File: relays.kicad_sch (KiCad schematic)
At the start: 8 parts, among them K1 J107F1AS123VDC.36, K2 J107F1AS123VDC.36, K3 J107F1AS123VDC.36, Q1 2N2222A, Q2 2N2222A, Q3 2N2222A

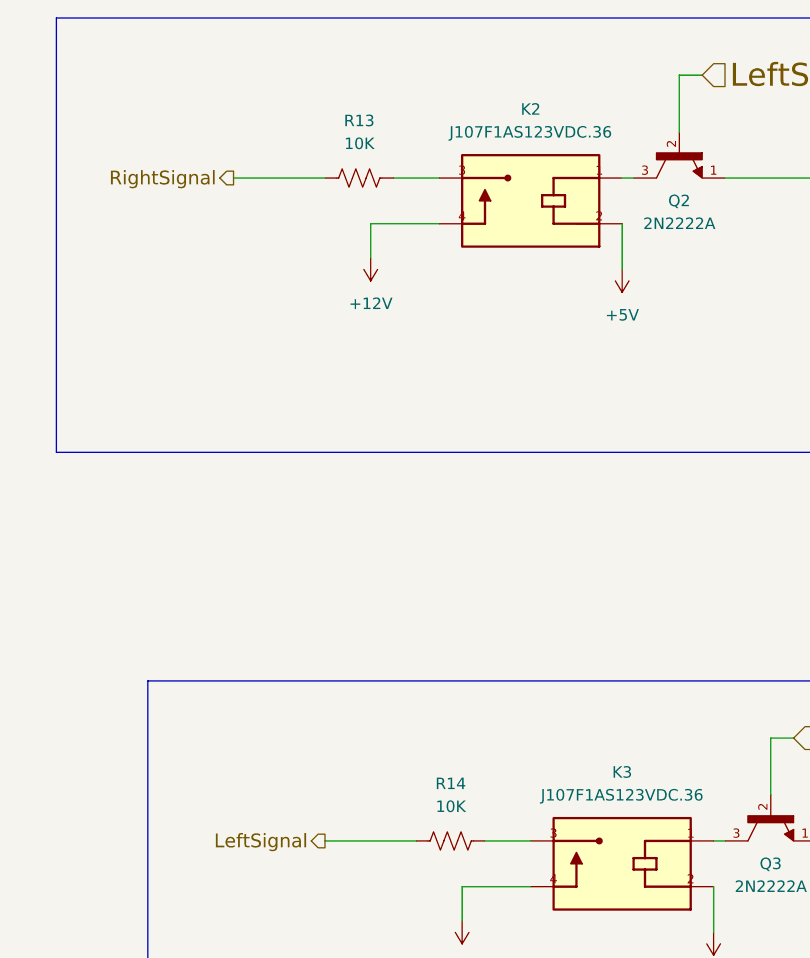
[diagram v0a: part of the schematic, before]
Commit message: placed most components
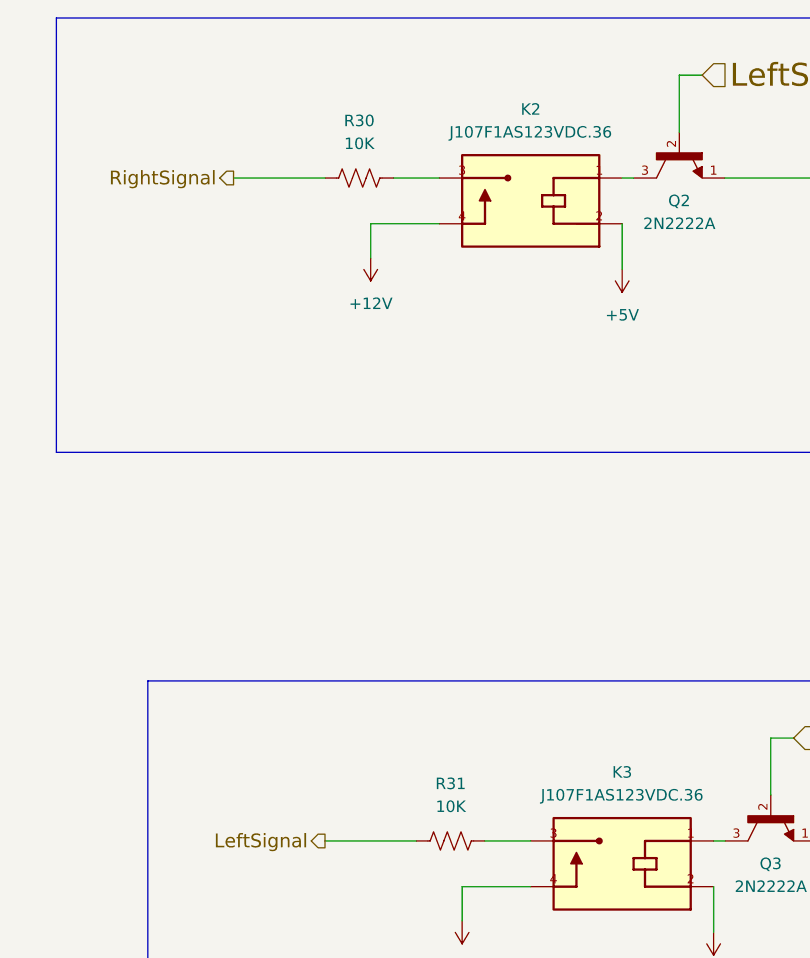
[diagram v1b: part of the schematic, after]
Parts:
- R30: renamed from R13; footprint (none) -> Resistor_SMD:R_0805_2012Metric
- R31: renamed from R14; footprint (none) -> Resistor_SMD:R_0805_2012Metric
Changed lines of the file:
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@@
 		(dnp no)
 		(fields_autoplaced yes)
-		(property "Reference" "#PWR023"
+		(property "Reference" "#PWR051"
 			(at 86.36 55.88 0)
 			(effects
@@
 			(project "Main-Board-V2"
 				(path "/c01682a2-308a-4674-9b8f-80e441c05d08/21d63675-f3e4-4d8d-ac51-eab9a4aeae5e"
-					(reference "#PWR023")
+					(reference "#PWR051")
 					(unit 1)
 				)
@@
 		(dnp no)
 		(fields_autoplaced yes)
-		(property "Reference" "#PWR025"
+		(property "Reference" "#PWR052"
 			(at 109.22 59.69 0)
 			(effects
@@
 			(project "Main-Board-V2"
 				(path "/c01682a2-308a-4674-9b8f-80e441c05d08/21d63675-f3e4-4d8d-ac51-eab9a4aeae5e"
-					(reference "#PWR025")
+					(reference "#PWR052")
 					(unit 1)
 				)
@@
 		(dnp no)
 		(fields_autoplaced yes)
-		(property "Reference" "R13"
+		(property "Reference" "R30"
 			(at 185.42 41.91 90)
 			(effects
@@
 			)
 		)
-		(property "Footprint" ""
+		(property "Footprint" "Resistor_SMD:R_0805_2012Metric"
 			(at 185.674 47.244 90)
 			(effects
@@
 			(project "Main-Board-V2"
 				(path "/c01682a2-308a-4674-9b8f-80e441c05d08/21d63675-f3e4-4d8d-ac51-eab9a4aeae5e"
-					(reference "R13")
+					(reference "R30")
 					(unit 1)
 				)
@@
 		(dnp no)
 		(fields_autoplaced yes)
-		(property "Reference" "#PWR029"
+		(property "Reference" "#PWR056"
 			(at 224.79 128.27 0)
 			(effects
@@
 			(project "Main-Board-V2"
 				(path "/c01682a2-308a-4674-9b8f-80e441c05d08/21d63675-f3e4-4d8d-ac51-eab9a4aeae5e"
-					(reference "#PWR029")
+					(reference "#PWR056")
 					(unit 1)
 				)
@@
 		(dnp no)
 		(fields_autoplaced yes)
-		(property "Reference" "#PWR044"
+		(property "Reference" "#PWR057"
 			(at 237.49 58.42 0)
 			(effects
@@
 			(project "Main-Board-V2"
 				(path "/c01682a2-308a-4674-9b8f-80e441c05d08/21d63675-f3e4-4d8d-ac51-eab9a4aeae5e"
-					(reference "#PWR044")
+					(reference "#PWR057")
 					(unit 1)
 				)
@@
 		(dnp no)
 		(fields_autoplaced yes)
-		(property "Reference" "#PWR028"
+		(property "Reference" "#PWR055"
 			(at 214.63 54.61 0)
 			(effects
@@
 			(project "Main-Board-V2"
 				(path "/c01682a2-308a-4674-9b8f-80e441c05d08/21d63675-f3e4-4d8d-ac51-eab9a4aeae5e"
-					(reference "#PWR028")
+					(reference "#PWR055")
 					(unit 1)
 				)
@@
 		(dnp no)
 		(fields_autoplaced yes)
-		(property "Reference" "#PWR045"
+		(property "Reference" "#PWR058"
 			(at 247.65 132.08 0)
 			(effects
@@
 			(project "Main-Board-V2"
 				(path "/c01682a2-308a-4674-9b8f-80e441c05d08/21d63675-f3e4-4d8d-ac51-eab9a4aeae5e"
-					(reference "#PWR045")
+					(reference "#PWR058")
 					(unit 1)
 				)
@@
 		(dnp no)
 		(fields_autoplaced yes)
-		(property "Reference" "R14"
+		(property "Reference" "R31"
 			(at 195.58 115.57 90)
 			(effects
@@
 			)
 		)
-		(property "Footprint" ""
+		(property "Footprint" "Resistor_SMD:R_0805_2012Metric"
 			(at 195.834 120.904 90)
 			(effects
@@
 			(project "Main-Board-V2"
 				(path "/c01682a2-308a-4674-9b8f-80e441c05d08/21d63675-f3e4-4d8d-ac51-eab9a4aeae5e"
-					(reference "R14")
+					(reference "R31")
 					(unit 1)
 				)
@@
 		(dnp no)
 		(fields_autoplaced yes)
-		(property "Reference" "#PWR026"
+		(property "Reference" "#PWR053"
 			(at 186.69 53.34 0)
 			(effects
@@
 			(project "Main-Board-V2"
 				(path "/c01682a2-308a-4674-9b8f-80e441c05d08/21d63675-f3e4-4d8d-ac51-eab9a4aeae5e"
-					(reference "#PWR026")
+					(reference "#PWR053")
 					(unit 1)
 				)
@@
 		(dnp no)
 		(fields_autoplaced yes)
-		(property "Reference" "#PWR027"
+		(property "Reference" "#PWR054"
 			(at 196.85 127 0)
 			(effects
@@
 			(project "Main-Board-V2"
 				(path "/c01682a2-308a-4674-9b8f-80e441c05d08/21d63675-f3e4-4d8d-ac51-eab9a4aeae5e"
-					(reference "#PWR027")
+					(reference "#PWR054")
 					(unit 1)
 				)

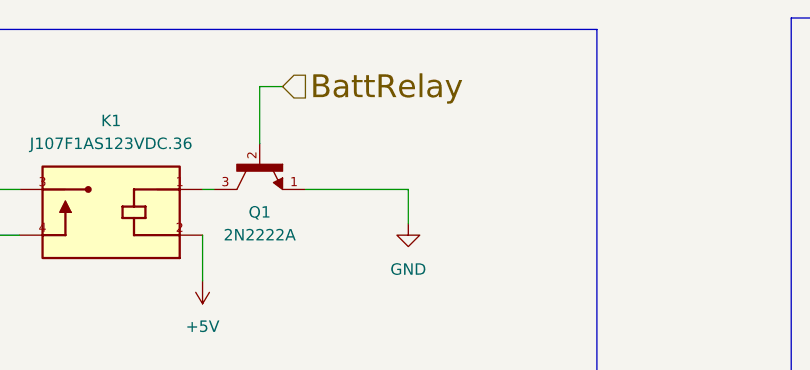
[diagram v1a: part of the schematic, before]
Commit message: replaced CAN chip, power planes
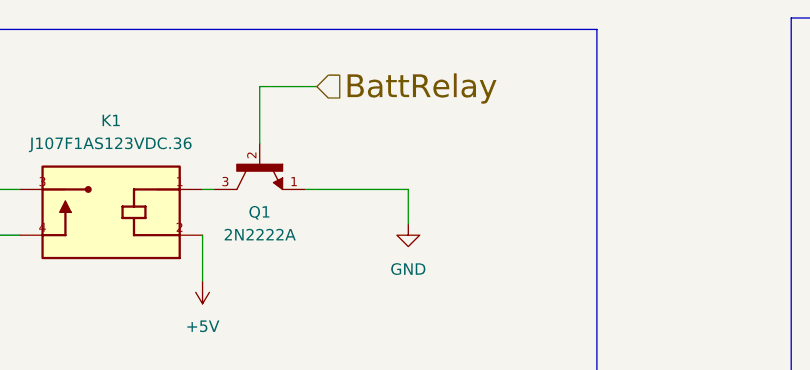
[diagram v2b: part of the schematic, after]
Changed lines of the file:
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@@
 	(wire
 		(pts
-			(xy 92.71 38.1) (xy 95.25 38.1)
+			(xy 92.71 38.1) (xy 99.06 38.1)
 		)
 		(stroke
@@
 	(hierarchical_label "BattRelay"
 		(shape input)
-		(at 95.25 38.1 0)
+		(at 99.06 38.1 0)
 		(effects
 			(font

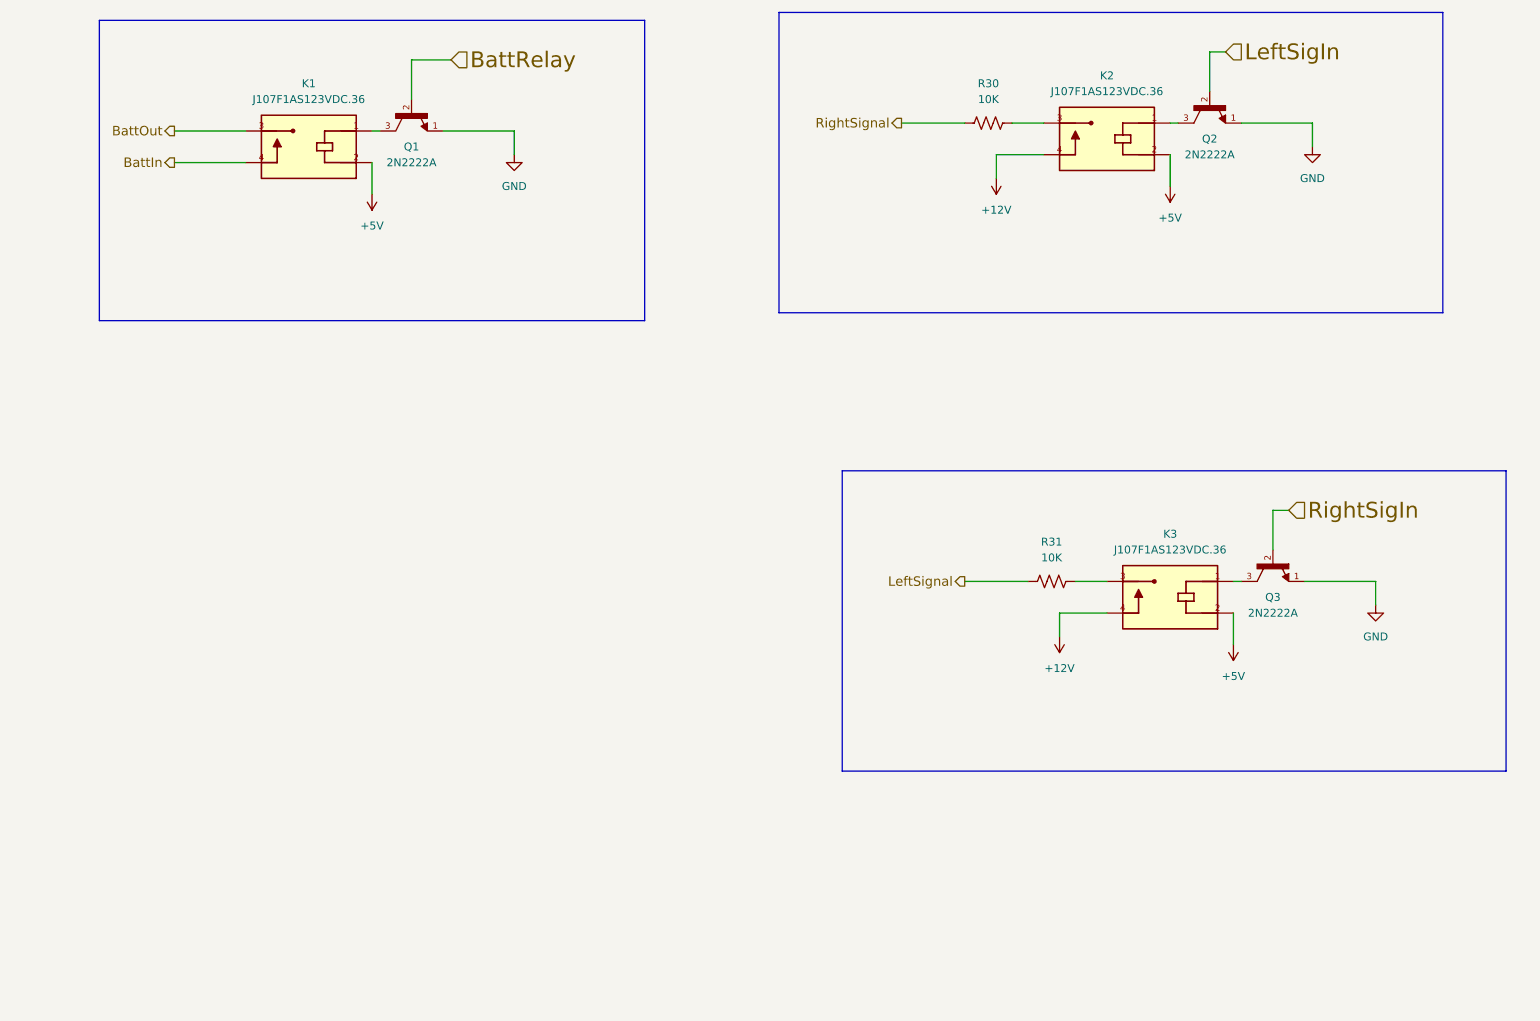
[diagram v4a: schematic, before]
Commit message: redid 35 pos pinout
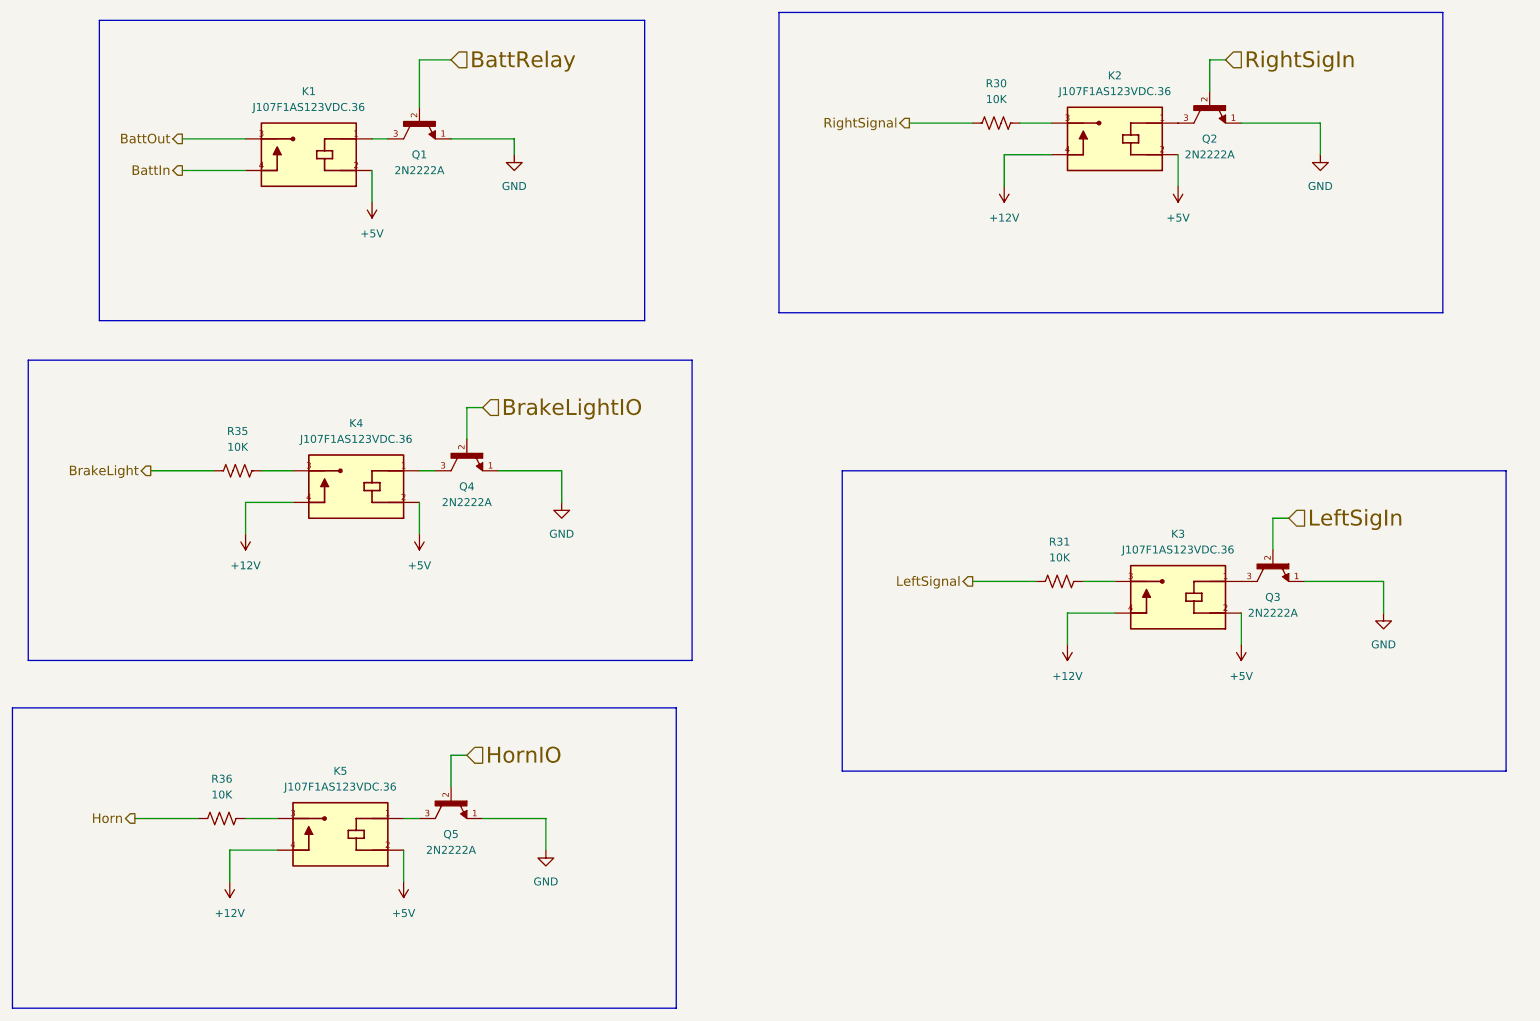
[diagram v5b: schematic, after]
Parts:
- added K4, K5: J107F1AS123VDC.36, PRE29-5V-S-450-1A-E:RELAY_PRE29-5V-S-450-1A-E, symbol PRE29-5V-S-450-1A-E:PRE29-5V-S-450-1A-E
- added Q4, Q5: 2N2222A, 2N2222A:TO92254P470H750-3, symbol 2N2222A:2N2222A
- added R35, R36: 10K, Resistor_SMD:R_0805_2012Metric, symbol Device:R_US
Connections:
- net +12V: now also K4.4, K5.4
- net +5V: now also K4.2, K5.2
- net GND: now also Q4.1, Q5.1
- net LeftSigIn: now also Q3.2; no longer Q2.2
- net RightSigIn: now also Q2.2; no longer Q3.2
- new net: K5.1, Q5.3
- new net: K5.3, R36.2
- new net: K4.1, Q4.3
- new net: K4.3, R35.2
- new net BrakeLight: R35.1
- new net BrakeLightIO: Q4.2
- new net Horn: R36.1
- new net HornIO: Q5.2
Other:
- moved on the sheet: K1, K2, K3, Q1, R30, R31

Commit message: complete. Minor Tweaks
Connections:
- net BattIn: now also K1.3; no longer K1.4
- net BattOut: now also K1.4; no longer K1.3
- net BrakeLight: now also R31.1; no longer R35.1
- net LeftSignal: now also R30.1; no longer R31.1
- net RightSignal: now also R35.1; no longer R30.1
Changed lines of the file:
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@@
 	(hierarchical_label "LeftSignal"
 		(shape output)
-		(at 182.88 121.92 180)
+		(at 172.72 48.26 180)
 		(effects
 			(font
@@
 	(hierarchical_label "BattIn"
 		(shape output)
-		(at 55.88 55.88 180)
-		(effects
-			(font
-				(size 1.524 1.524)
-			)
-			(justify right)
-		)
-	)
-	(hierarchical_label "RightSignal"
-		(shape output)
-		(at 172.72 48.26 180)
-		(effects
-			(font
-				(size 1.524 1.524)
-			)
-			(justify right)
-		)
-	)
-	(hierarchical_label "BrakeLight"
-		(shape output)
-		(at 50.8 104.14 180)
+		(at 55.88 50.8 180)
 		(effects
 			(font
@@
 		)
 	)
+	(hierarchical_label "BattOut"
+		(shape output)
+		(at 55.88 55.88 180)
+		(effects
+			(font
+				(size 1.524 1.524)
+			)
+			(justify right)
+		)
+	)
 	(hierarchical_label "BattRelay"
 		(shape input)
@@
 		)
 	)
-	(hierarchical_label "BattOut"
+	(hierarchical_label "RightSignal"
 		(shape output)
-		(at 55.88 50.8 180)
+		(at 50.8 104.14 180)
 		(effects
 			(font
@@
 		)
 	)
+	(hierarchical_label "BrakeLight"
+		(shape output)
+		(at 182.88 121.92 180)
+		(effects
+			(font
+				(size 1.524 1.524)
+			)
+			(justify right)
+		)
+	)

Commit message: removed resistors for light boards
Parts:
- removed R30, R31, R35: 10K, Resistor_SMD:R_0805_2012Metric, symbol Device:R_US
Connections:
- net BrakeLight: now also K3.3
- net BrakeLightIO: now also Q3.2; no longer Q4.2
- net LeftSigIn: now also Q2.2; no longer Q3.2
- net LeftSignal: now also K2.3
- net RightSigIn: now also Q4.2; no longer Q2.2
- net RightSignal: now also K4.3
